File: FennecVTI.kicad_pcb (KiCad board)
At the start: 2 copper layers, 218 x 131.9 mm, 88 parts, among them J1 Expansion Connector, J2 Slot Select, J3 Conn_Coaxial, J4 MDA/CGA connector, J5 DB15_Female, J6 DIP14 Keyboard Connector, J7 User Connector, Q1 2N3906, U1 74LS191, U10 74LS574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

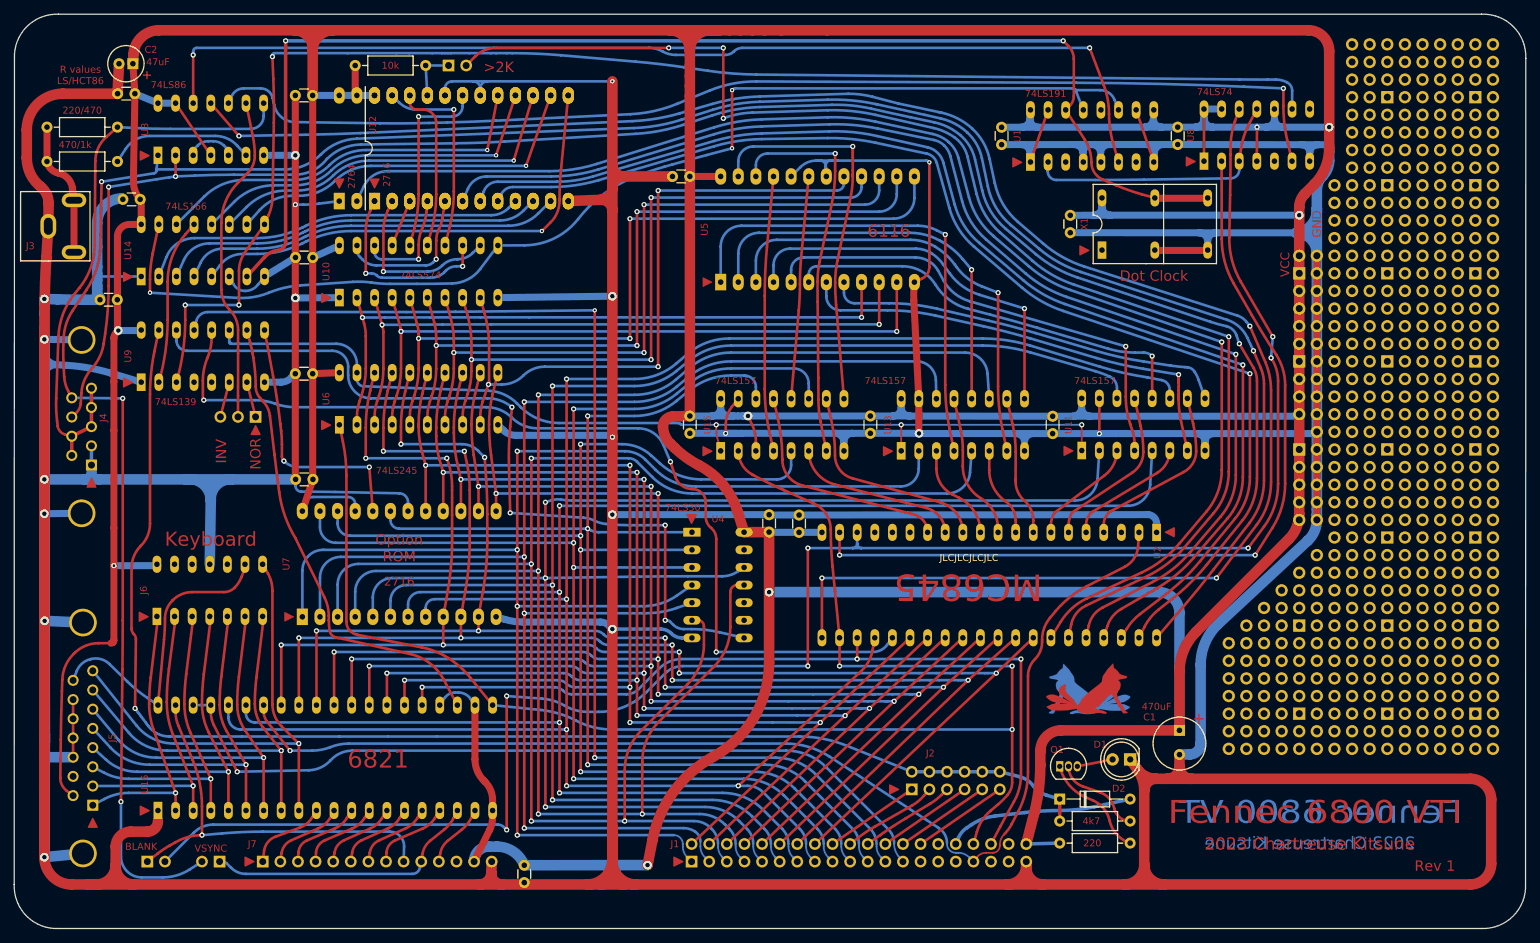
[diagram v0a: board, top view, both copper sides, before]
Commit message: Changed transistor footprint, removed some 0 length traces
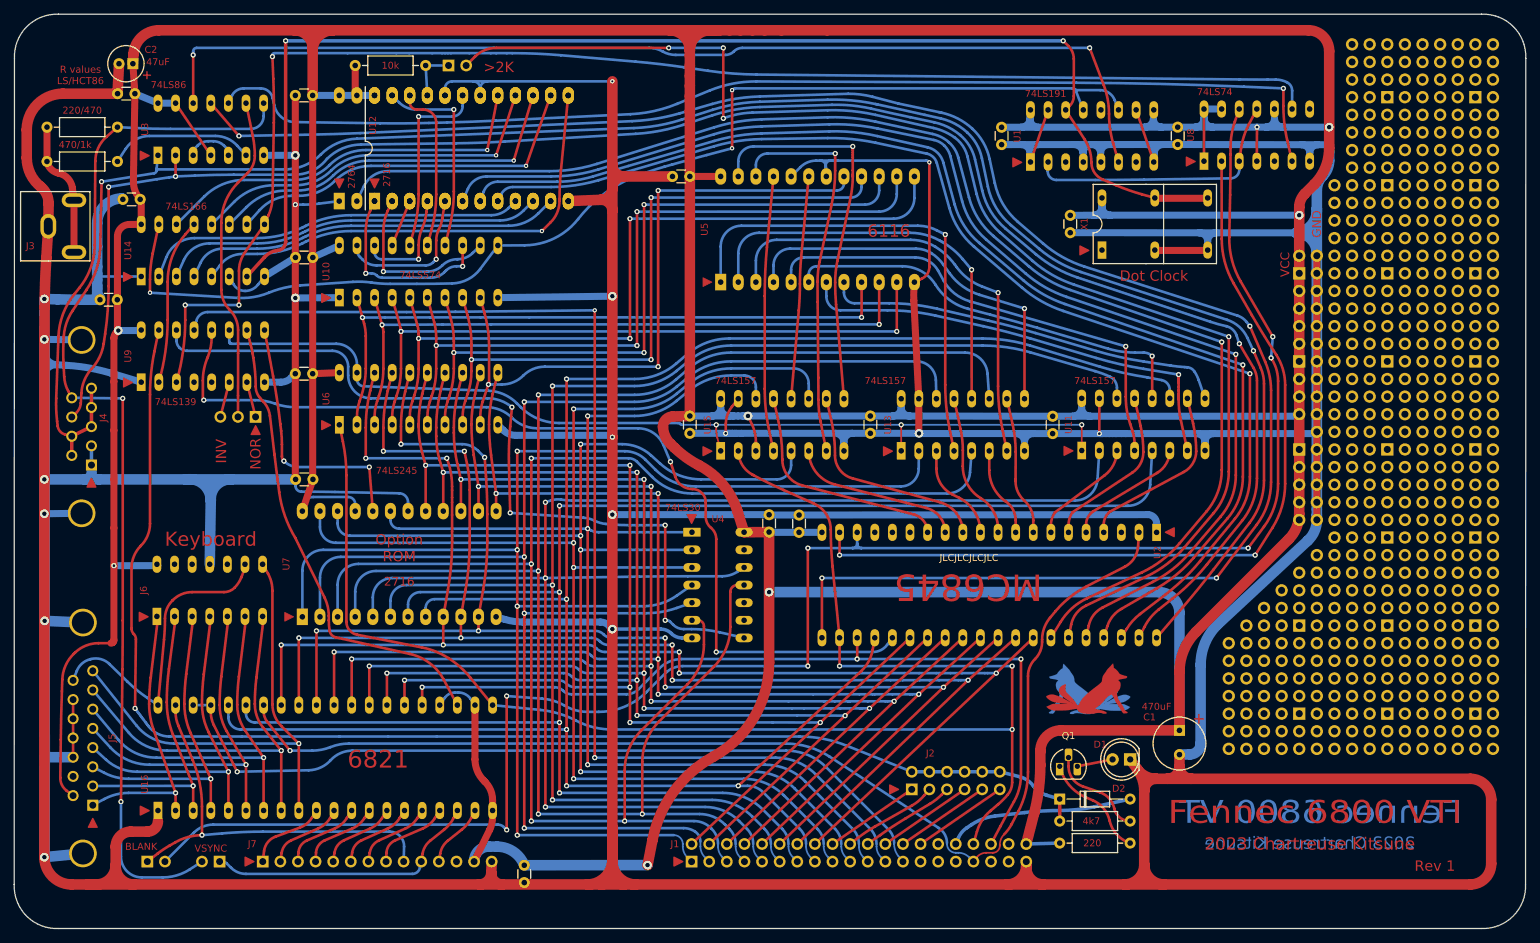
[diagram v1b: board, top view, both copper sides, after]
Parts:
- Q1: footprint Package_TO_SOT_THT:TO-92_Inline -> Package_TO_SOT_THT:TO-92_HandSolder
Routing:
- net GND: track 1602.5 -> 1600.8 mm
- net Net-(Q1-Pad2): track 12.7 -> 13.9 mm

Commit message: Added 2764 optional footprint for main rom. Rotated keyboard connector
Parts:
- added U70: 27128, Plain Sockets:DIP-28 Copper Ref Pin 1, F.Cu at (89.9, 104.9)
- R4: value 220/470 -> 220
- R5: value 470/1k -> 470
- moved J6 2.62 mm to (62.9, 107.3), turned to -90 degrees
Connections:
- J4 pad 0: GND -> (no net)
- J5 pad 0: GND -> (no net)
- U120 pad 1: GND -> unconnected-(U120-VPP-Pad1)
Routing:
- net VCC: track 1090.5 -> 1119.8 mm
- net /KEYD0: track 40.7 -> 56.6 mm
- net /KEYD1: track 42.9 -> 56.2 mm
- net /KEYD2: track 45.9 -> 56.3 mm
- net /KEYD7: track 71.2 -> 63.9 mm
- net /KEYD4: track 52.6 -> 59.9 mm, vias 1 -> 2
- net /KEYD3: track 49.2 -> 56.5 mm
- net /KEYD5: track 56.2 -> 62.9 mm, vias 1 -> 2
- net GND: track 1600.8 -> 1595.2 mm, vias 18 -> 17
- net /KEYSTROBE: track 44.7 -> 39.9 mm
- net /KEYD6: track 59.7 -> 64.5 mm, vias 1 -> 2
- net /~{PIACS}: track 68.4 -> 73.0 mm
- net BD0: track 209.7 -> 207.5 mm
- net BD1: track 205.1 -> 203.0 mm
- net BD2: track 200.1 -> 199.4 mm
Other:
- board text added: "HCT=470/1k"
- board text added: "R values for LS86"
- board text removed: "R values LS/HCT86"
